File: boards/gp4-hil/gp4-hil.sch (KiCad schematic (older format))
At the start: 0 parts

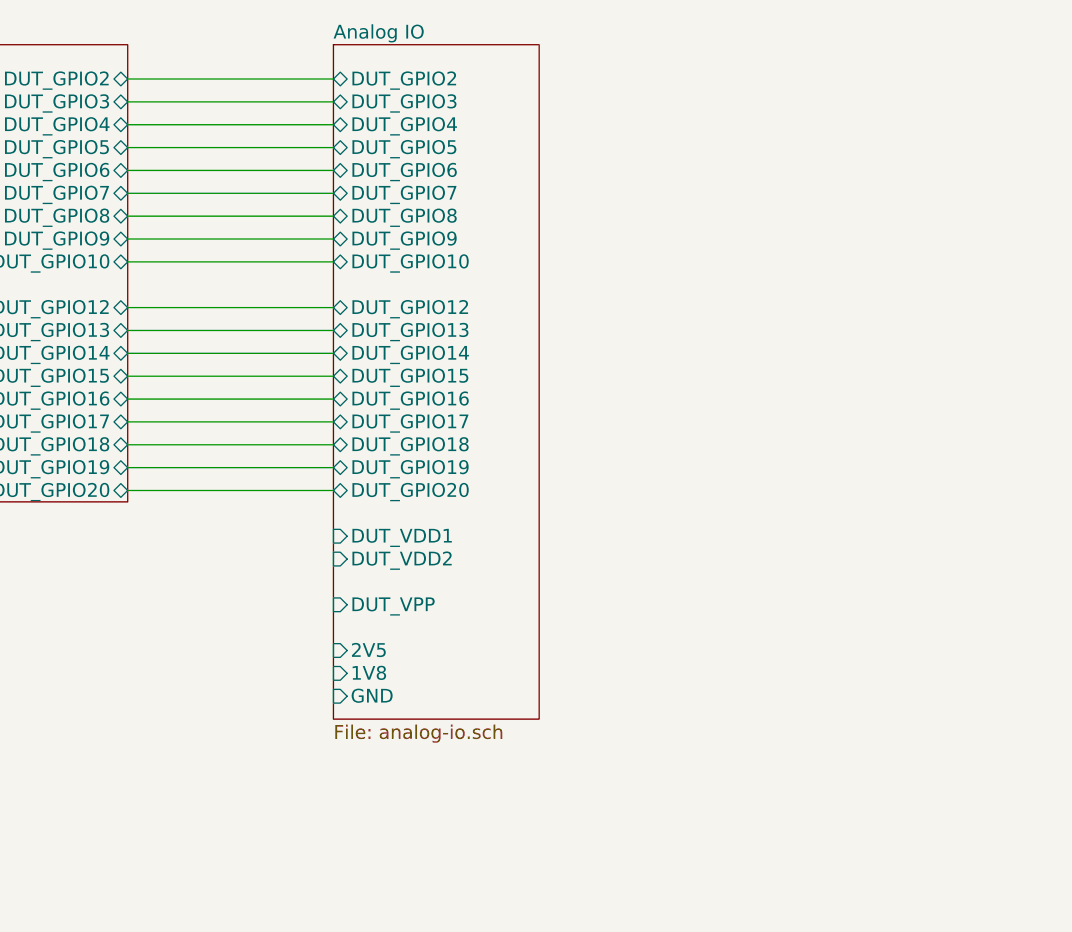
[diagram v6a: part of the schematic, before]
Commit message: Added digital IO schematic page, analog switches, and enable inputs.
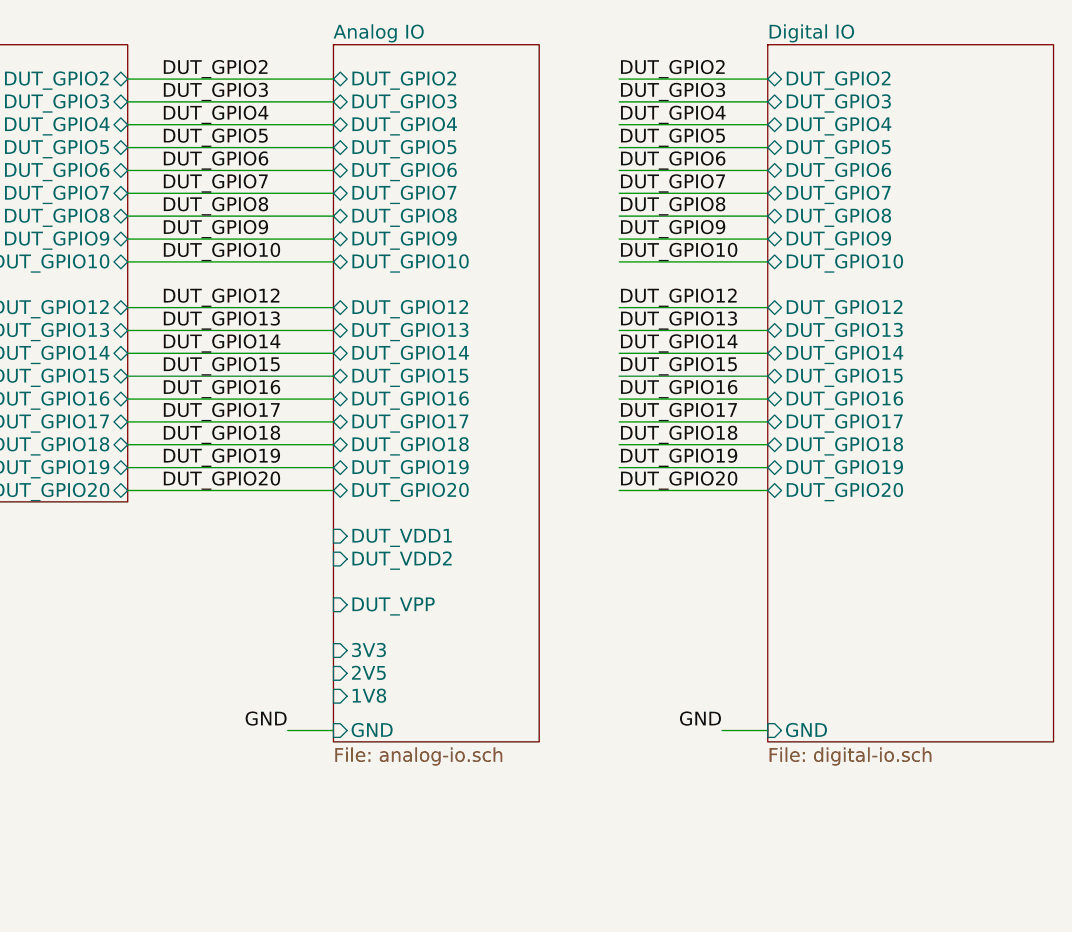
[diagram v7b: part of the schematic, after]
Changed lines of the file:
@@
 $Descr A2 23386 16535
 encoding utf-8
-Sheet 1 7
+Sheet 1 8
 Title "GreenPak Hardware-In-Loop Test Platform"
-Date "2016-05-13"
+Date "2016-05-14"
 Rev "0.1"
 Comp "Andrew Zonenberg"
@@
 $EndSheet
 $Sheet
-S 9000 1200 900  2950
+S 9000 1200 900  3050
 U 57316A68
 F0 "Analog IO" 60
@@
 F2 "DUT_VDD1" I L 9000 3350 60
 F3 "DUT_VDD2" I L 9000 3450 60
-F4 "GND" I L 9000 4050 60
+F4 "GND" I L 9000 4200 60
 F5 "DUT_VPP" I L 9000 3650 60
 F6 "DUT_GPIO2" B L 9000 1350 60
@@
 F22 "DUT_GPIO19" B L 9000 3050 60
 F23 "DUT_GPIO20" B L 9000 3150 60
-F24 "2V5" I L 9000 3850 60
-F25 "1V8" I L 9000 3950 60
+F24 "2V5" I L 9000 3950 60
+F25 "1V8" I L 9000 4050 60
+F26 "3V3" I L 9000 3850 60
 $EndSheet
 $Sheet
@@
 Text Notes 1500 7150 0    60   ~ 0
 Possibly the most overkill dev board ever.\n* Target device has 26 LUTs and 12 FFs\n* Support FPGA has 63,400 LUTs and 126800 FFs (if you load the 100t)\n* Has an ADC, DAC, and digital I/O on every pin of the DUT, all bridged out to TCP sockets\n* TCP programming, simply netcat a bitstream to the board to flash the DUT
+Text Label 8250 1350 0    60   ~ 0
+DUT_GPIO2
+Text Label 8250 1450 0    60   ~ 0
+DUT_GPIO3
+Text Label 8250 1550 0    60   ~ 0
+DUT_GPIO4
+Text Label 8250 1650 0    60   ~ 0
+DUT_GPIO5
+Text Label 8250 1750 0    60   ~ 0
+DUT_GPIO6
+Text Label 8250 1850 0    60   ~ 0
+DUT_GPIO7
+Text Label 8250 1950 0    60   ~ 0
+DUT_GPIO8
+Text Label 8250 2050 0    60   ~ 0
+DUT_GPIO9
+Text Label 8250 2150 0    60   ~ 0
+DUT_GPIO10
+Text Label 8250 2350 0    60   ~ 0
+DUT_GPIO12
+Text Label 8250 2450 0    60   ~ 0
+DUT_GPIO13
+Text Label 8250 2550 0    60   ~ 0
+DUT_GPIO14
+Text Label 8250 2650 0    60   ~ 0
+DUT_GPIO15
+Text Label 8250 2750 0    60   ~ 0
+DUT_GPIO16
+Text Label 8250 2850 0    60   ~ 0
+DUT_GPIO17
+Text Label 8250 2950 0    60   ~ 0
+DUT_GPIO18
+Text Label 8250 3050 0    60   ~ 0
+DUT_GPIO19
+Text Label 8250 3150 0    60   ~ 0
+DUT_GPIO20
+$Sheet
+S 10900 1200 1250 3050
+U 573AABB3
+F0 "Digital IO" 60
+F1 "digital-io.sch" 60
+F2 "GND" I L 10900 4200 60
+F3 "DUT_GPIO2" B L 10900 1350 60
+F4 "DUT_GPIO3" B L 10900 1450 60
+F5 "DUT_GPIO4" B L 10900 1550 60
+F6 "DUT_GPIO5" B L 10900 1650 60
+F7 "DUT_GPIO6" B L 10900 1750 60
+F8 "DUT_GPIO7" B L 10900 1850 60
+F9 "DUT_GPIO8" B L 10900 1950 60
+F10 "DUT_GPIO9" B L 10900 2050 60
+F11 "DUT_GPIO10" B L 10900 2150 60
+F12 "DUT_GPIO12" B L 10900 2350 60
+F13 "DUT_GPIO13" B L 10900 2450 60
+F14 "DUT_GPIO14" B L 10900 2550 60
+F15 "DUT_GPIO15" B L 10900 2650 60
+F16 "DUT_GPIO16" B L 10900 2750 60
+F17 "DUT_GPIO17" B L 10900 2850 60
+F18 "DUT_GPIO18" B L 10900 2950 60
+F19 "DUT_GPIO19" B L 10900 3050 60
+F20 "DUT_GPIO20" B L 10900 3150 60
+$EndSheet
+Text Label 10250 1350 0    60   ~ 0
+DUT_GPIO2
+Text Label 10250 1450 0    60   ~ 0
+DUT_GPIO3
+Text Label 10250 1550 0    60   ~ 0
+DUT_GPIO4
+Text Label 10250 1650 0    60   ~ 0
+DUT_GPIO5
+Text Label 10250 1750 0    60   ~ 0
+DUT_GPIO6
+Text Label 10250 1850 0    60   ~ 0
+DUT_GPIO7
+Text Label 10250 1950 0    60   ~ 0
+DUT_GPIO8
+Text Label 10250 2050 0    60   ~ 0
+DUT_GPIO9
+Text Label 10250 2150 0    60   ~ 0
+DUT_GPIO10
+Text Label 10250 2350 0    60   ~ 0
+DUT_GPIO12
+Text Label 10250 2450 0    60   ~ 0
+DUT_GPIO13
+Text Label 10250 2550 0    60   ~ 0
+DUT_GPIO14
+Text Label 10250 2650 0    60   ~ 0
+DUT_GPIO15
+Text Label 10250 2750 0    60   ~ 0
+DUT_GPIO16
+Text Label 10250 2850 0    60   ~ 0
+DUT_GPIO17
+Text Label 10250 2950 0    60   ~ 0
+DUT_GPIO18
+Text Label 10250 3050 0    60   ~ 0
+DUT_GPIO19
+Text Label 10250 3150 0    60   ~ 0
+DUT_GPIO20
+Wire Wire Line
+	10250 1350 10900 1350
+Wire Wire Line
+	10900 1450 10250 1450
+Wire Wire Line
+	10250 1550 10900 1550
+Wire Wire Line
+	10900 1650 10250 1650
+Wire Wire Line
+	10250 1750 10900 1750
+Wire Wire Line
+	10900 1850 10250 1850
+Wire Wire Line
+	10250 1950 10900 1950
+Wire Wire Line
+	10900 2050 10250 2050
+Wire Wire Line
+	10250 2150 10900 2150
+Wire Wire Line
+	10900 2350 10250 2350
+Wire Wire Line
+	10900 2450 10250 2450
+Wire Wire Line
+	10900 2550 10250 2550
+Wire Wire Line
+	10250 2650 10900 2650
+Wire Wire Line
+	10900 2750 10250 2750
+Wire Wire Line
+	10900 2850 10250 2850
+Wire Wire Line
+	10250 2950 10900 2950
+Wire Wire Line
+	10900 3050 10250 3050
+Wire Wire Line
+	10250 3150 10900 3150
+Text Label 10700 4200 2    60   ~ 0
+GND
+Wire Wire Line
+	10700 4200 10900 4200
+Text Label 8800 4200 2    60   ~ 0
+GND
+Wire Wire Line
+	8800 4200 9000 4200
 $EndSCHEMATC

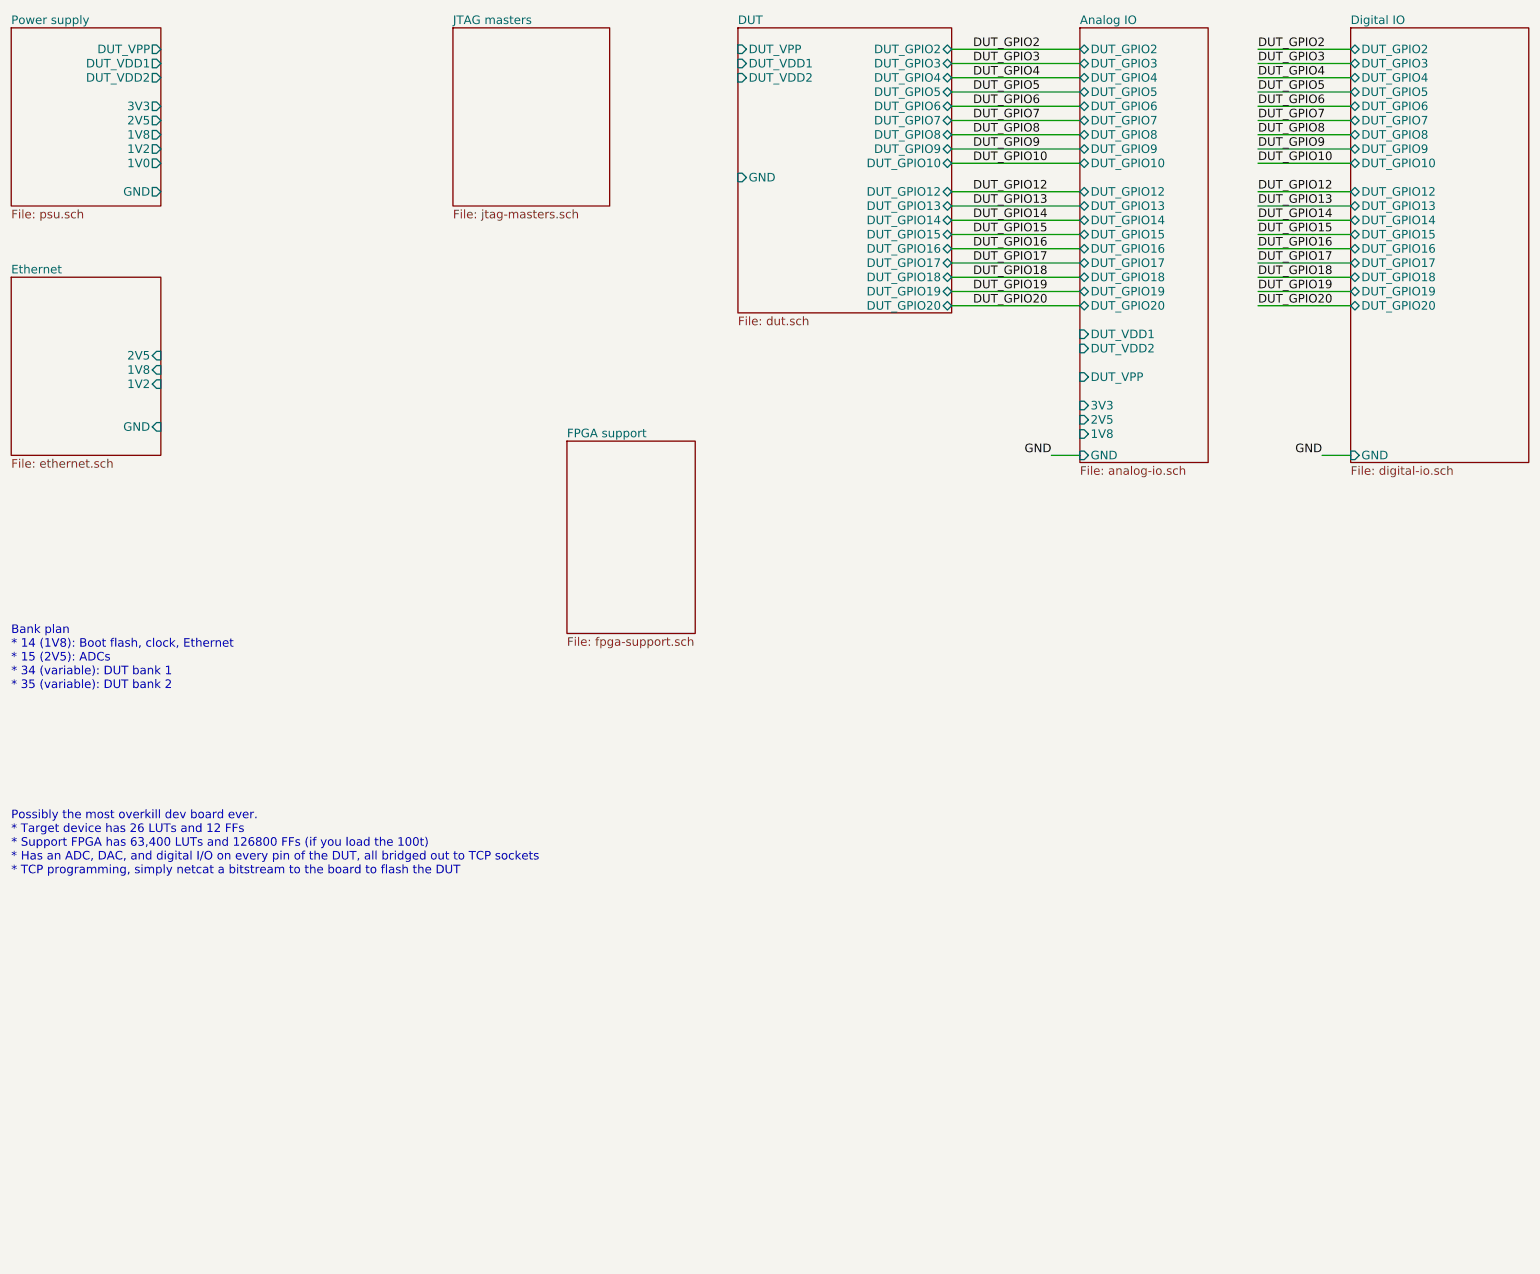
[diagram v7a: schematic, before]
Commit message: Schematic entry for 1V0 PSU
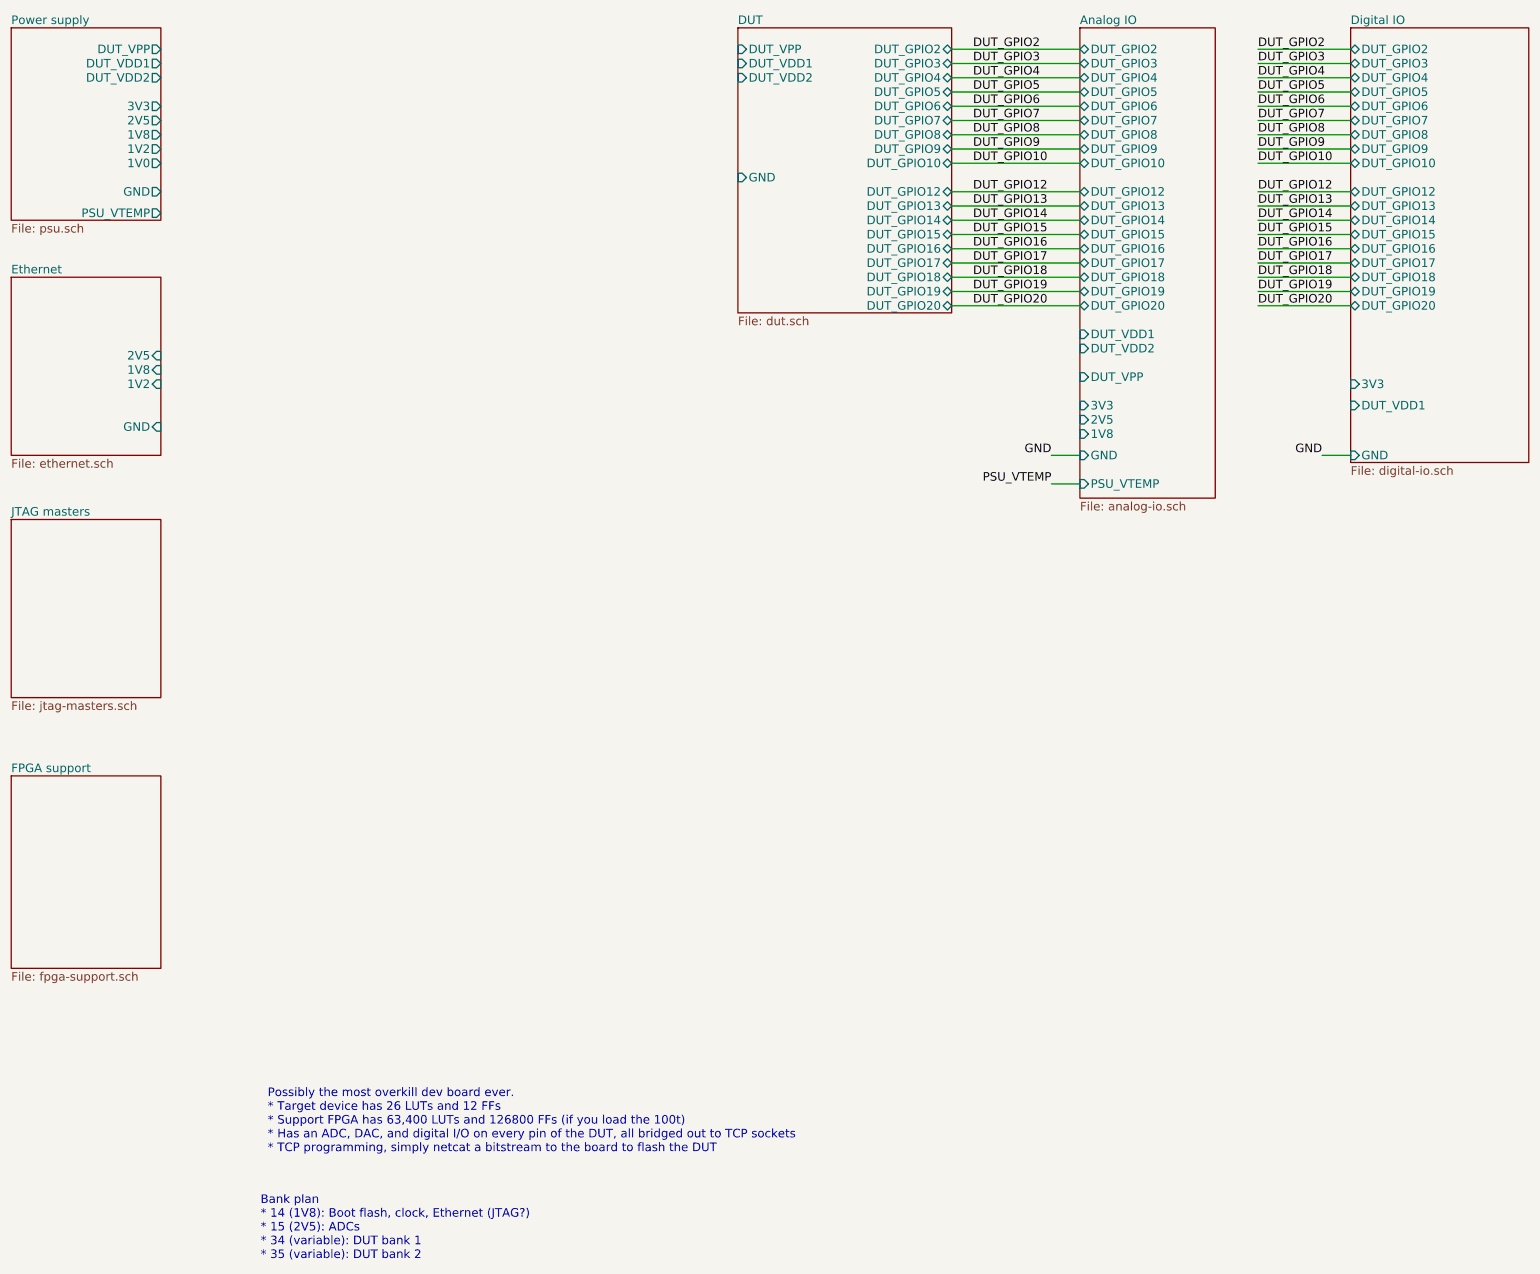
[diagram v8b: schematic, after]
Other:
- note added: "Bank plan\n* 14 (1V8): Boot flash, clock, Ethernet (JTAG?)\n* 15 (2V5): ADCs\n* 34 (variable): DUT bank 1\n* 35 (variable): DUT bank 2"
- note removed: "Bank plan\n* 14 (1V8): Boot flash, clock, Ethernet\n* 15 (2V5): ADCs\n* 34 (variable): DUT bank 1\n* 35 (variable): DUT bank 2"
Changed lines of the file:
@@
 Sheet 1 8
 Title "GreenPak Hardware-In-Loop Test Platform"
-Date "2016-05-14"
+Date "2016-05-15"
 Rev "0.1"
 Comp "Andrew Zonenberg"
@@
 $EndDescr
 $Sheet
-S 1500 1200 1050 1250
+S 1500 1200 1050 1350
 U 57316A38
 F0 "Power supply" 60
@@
 F9 "DUT_VDD2" O R 2550 1550 60
 F10 "3V3" O R 2550 1750 60
+F11 "PSU_VTEMP" O R 2550 2500 60
 $EndSheet
 $Sheet
@@
 $EndSheet
 $Sheet
-S 4600 1200 1100 1250
+S 1500 4650 1050 1250
 U 57316A4B
 F0 "JTAG masters" 60
@@
 $EndSheet
 $Sheet
-S 9000 1200 900  3050
+S 9000 1200 950  3300
 U 57316A68
 F0 "Analog IO" 60
@@
 F25 "1V8" I L 9000 4050 60
 F26 "3V3" I L 9000 3850 60
-$EndSheet
-$Sheet
-S 5400 4100 900  1350
+F27 "PSU_VTEMP" I L 9000 4400 60
+$EndSheet
+$Sheet
+S 1500 6450 1050 1350
 U 57316B0C
 F0 "FPGA support" 60
 F1 "fpga-support.sch" 60
 $EndSheet
-Text Notes 1500 5850 0    60   ~ 0
-Bank plan\n* 14 (1V8): Boot flash, clock, Ethernet\n* 15 (2V5): ADCs\n* 34 (variable): DUT bank 1\n* 35 (variable): DUT bank 2
+Text Notes 3250 9850 0    60   ~ 0
+Bank plan\n* 14 (1V8): Boot flash, clock, Ethernet (JTAG?)\n* 15 (2V5): ADCs\n* 34 (variable): DUT bank 1\n* 35 (variable): DUT bank 2
 Wire Wire Line
 	8100 1350 9000 1350
@@
 Wire Wire Line
 	9000 3150 8100 3150
-Text Notes 1500 7150 0    60   ~ 0
+Text Notes 3300 9100 0    60   ~ 0
 Possibly the most overkill dev board ever.\n* Target device has 26 LUTs and 12 FFs\n* Support FPGA has 63,400 LUTs and 126800 FFs (if you load the 100t)\n* Has an ADC, DAC, and digital I/O on every pin of the DUT, all bridged out to TCP sockets\n* TCP programming, simply netcat a bitstream to the board to flash the DUT
 Text Label 8250 1350 0    60   ~ 0
@@
 F19 "DUT_GPIO19" B L 10900 3050 60
 F20 "DUT_GPIO20" B L 10900 3150 60
+F21 "DUT_VDD1" I L 10900 3850 60
+F22 "3V3" I L 10900 3700 60
 $EndSheet
 Text Label 10250 1350 0    60   ~ 0
@@
 Wire Wire Line
 	8800 4200 9000 4200
+Text Label 8800 4400 2    60   ~ 0
+PSU_VTEMP
+Wire Wire Line
+	8800 4400 9000 4400
 $EndSCHEMATC
